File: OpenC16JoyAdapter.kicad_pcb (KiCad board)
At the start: 2 copper layers, 30.5 x 42.9 mm, 9 parts, among them J1 DB9 Male, P1 TO_C16_MINI_DIN_8, P2 PIN5_POWER, P3 OSHW_LOGO_PLACEHOLDER, P4 PULL_UP, U1 74LS244

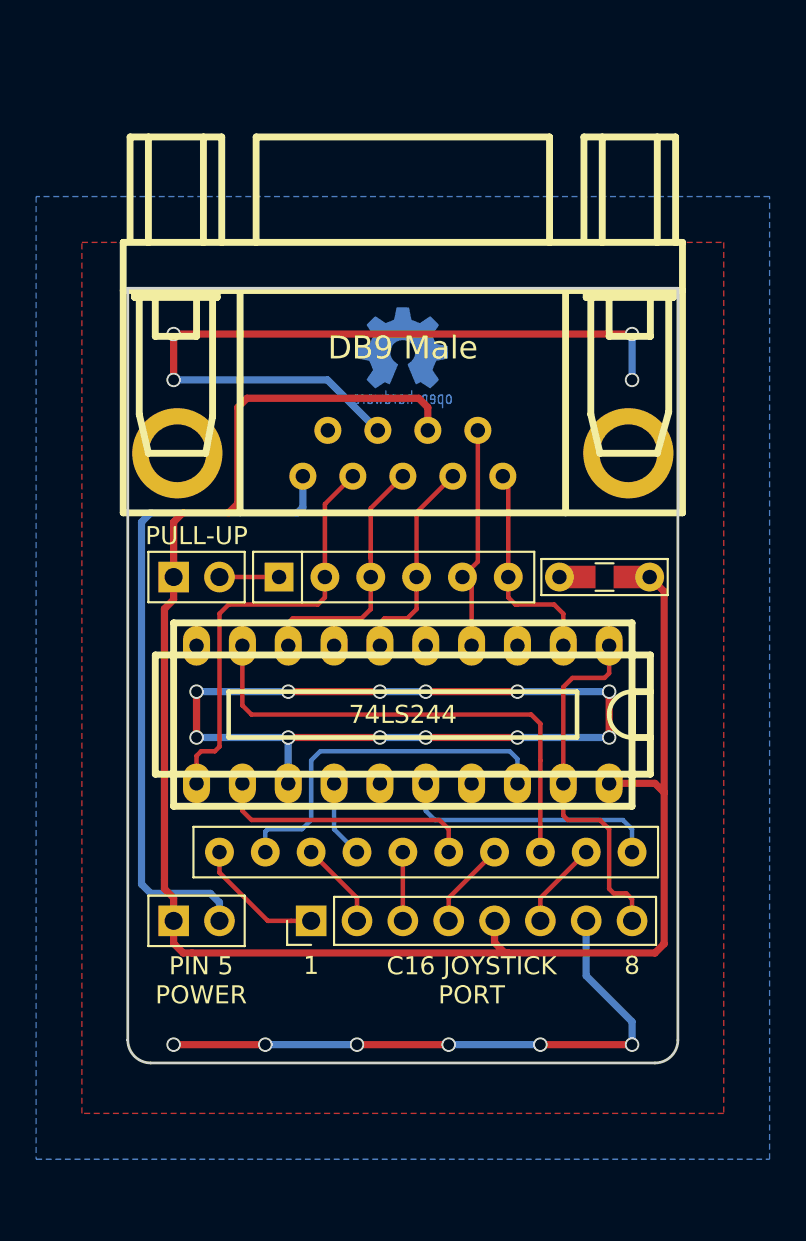
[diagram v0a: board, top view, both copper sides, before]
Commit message: Port to KiCad 5, remove pull-up jumper, tidy up, improve routing
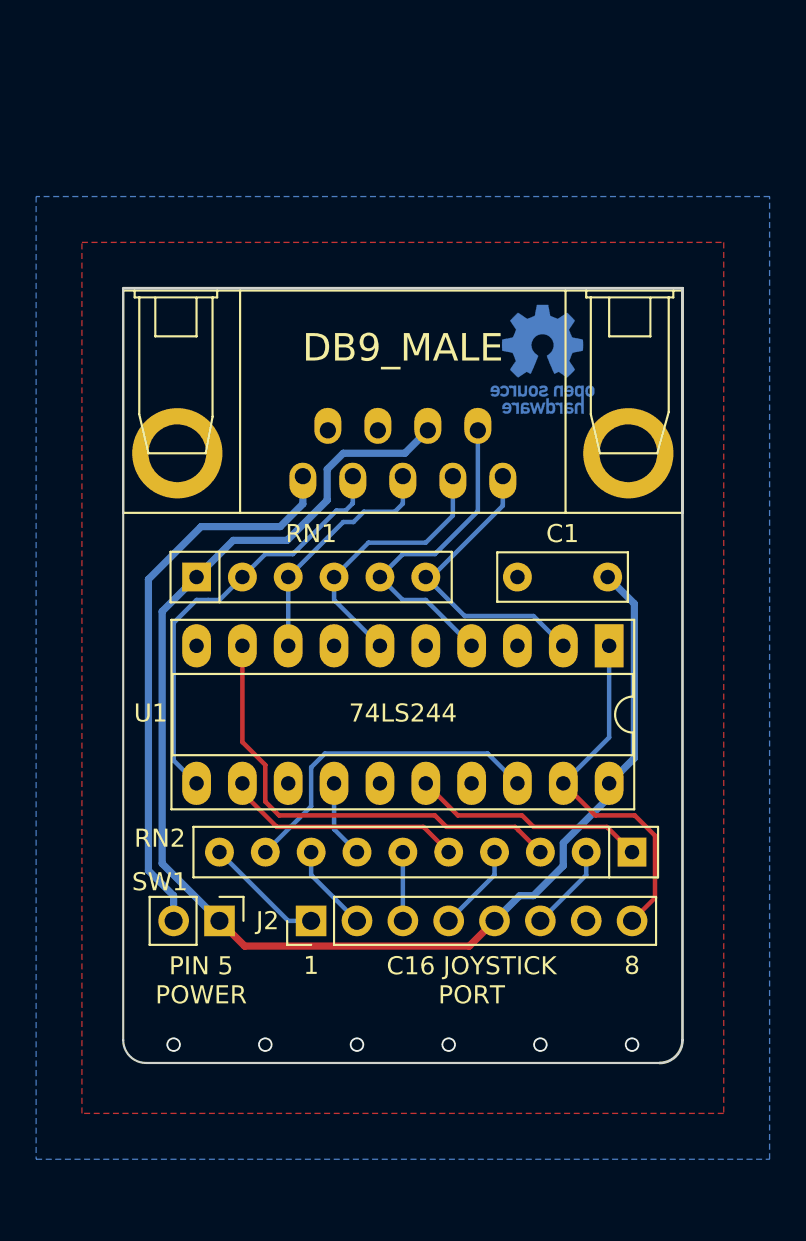
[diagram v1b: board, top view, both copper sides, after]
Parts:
- removed P1: TO_C16_MINI_DIN_8, Pin_Headers:Pin_Header_Straight_1x08_Pitch2.54mm
- removed P2: PIN5_POWER, OpenC16JoyAdapter:Pin_Header_Straight_1x02-ModSilkS
- removed P3: OSHW_LOGO_PLACEHOLDER, w_logo:Logo_copper_OSHW_6x6mm
- removed P4: PULL_UP, OpenC16JoyAdapter:Pin_Header_Straight_1x02-ModSilkS
- added J2: TO_C16_MINI_DIN_8, Connector_PinHeader_2.54mm:PinHeader_1x08_P2.54mm_Vertical, F.Cu at (142.2, 126.5)
- added SW1: PIN5_POWER, Connector_PinHeader_2.54mm:PinHeader_1x02_P2.54mm_Vertical, F.Cu at (137.2, 126.5)
- added V0: OSHW_LOGO, Symbol:OSHW-Logo_5.7x6mm_Copper, B.Cu at (155.1, 95.4)
- C1: footprint OpenC16JoyAdapter:C_0805+THT -> Capacitor_THT:C_Disc_D7.0mm_W2.5mm_P5.00mm
- J1: value DB9 Male -> DB9_MALE; footprint conn_d-sub:DB_9M -> OpenC16JoyAdapter:DB_9M
- RN1: footprint Resistors_THT:R_Array_SIP6 -> Resistor_THT:R_Array_SIP6
- RN2: footprint OpenC16JoyAdapter:R_Array_SIP10_NoPin1Mark -> Resistor_THT:R_Array_SIP10
- U1: footprint pth_circuits:dil_20-300_socket -> Package_DIP:DIP-20_W7.62mm_Socket_LongPads
- moved U1 12.0 mm to (158.8, 111.3), turned to 270 degrees
- moved RN1 4.57 mm to (135.9, 107.4)
- moved C1 0.17 mm to (158.7, 107.4)
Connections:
- J1 pad 9: (no net) -> /md_c_start
- RN1 pad 1: Net-(P4-Pad2) -> +5V
- U1 pad 3: (no net) -> Net-(U1-Pad3)
- U1 pad 5: (no net) -> Net-(U1-Pad5)
- U1 pad 7: (no net) -> Net-(U1-Pad7)
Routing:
- net GND: track 129.6 -> 0.00 mm, vias 22 -> 6
- net +5V: track 100.3 -> 78.1 mm
- net /md_b_~a: track 12.5 -> 18.1 mm
- net Net-(J1-Pad5): track 36.8 -> 31.3 mm
- net /md_up: track 12.0 -> 16.7 mm
- net Net-(P4-Pad2): track 3.30 -> 0.00 mm
- net /md_down: track 11.8 -> 15.0 mm
- net Net-(RN2-Pad9): track 20.4 -> 18.2 mm
- net Net-(RN2-Pad3): track 27.3 -> 25.6 mm
- net Net-(RN2-Pad1): track 14.6 -> 13.0 mm
- net Net-(RN2-Pad5): track 14.6 -> 13.3 mm
- net /md_left: track 14.5 -> 13.4 mm
- net /c16_up: track 7.32 -> 6.66 mm
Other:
- board size 30.5 x 42.9 mm -> 31 x 42.9 mm
- board text added: "+5V"
- board text added: "D"
- board text added: "F"
- board text added: "GND"
- board text added: "L"
- board text added: "Licensed under CERN OHL v.1.2"
- board text added: "R"
- board text added: "SEL"
- board text added: "U"
- board text added: "V3"
- board text removed: "PULL-UP"
- board text removed: "V2"

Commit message: Minor changes
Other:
- board text added: "Thanks to Levente Hársfalvi (TLC)!"

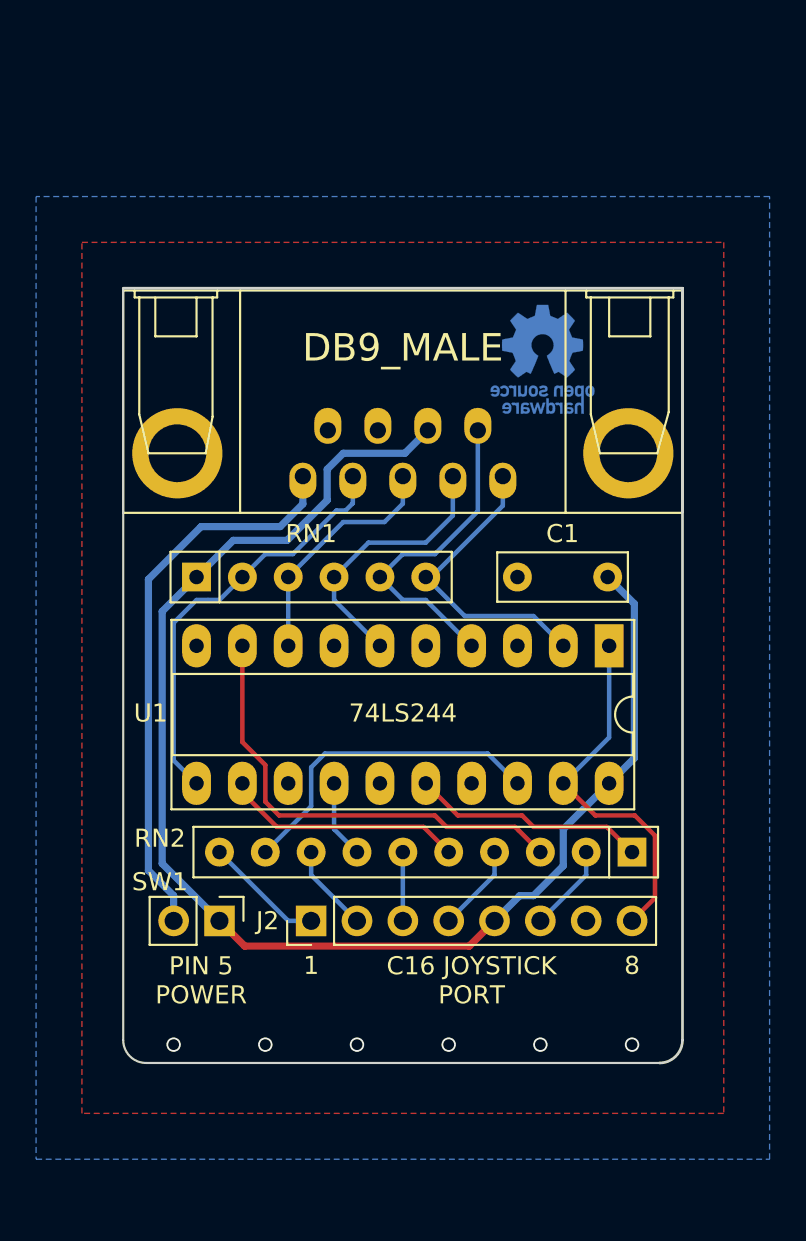
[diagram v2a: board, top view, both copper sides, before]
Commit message: Integrate light pen circuit
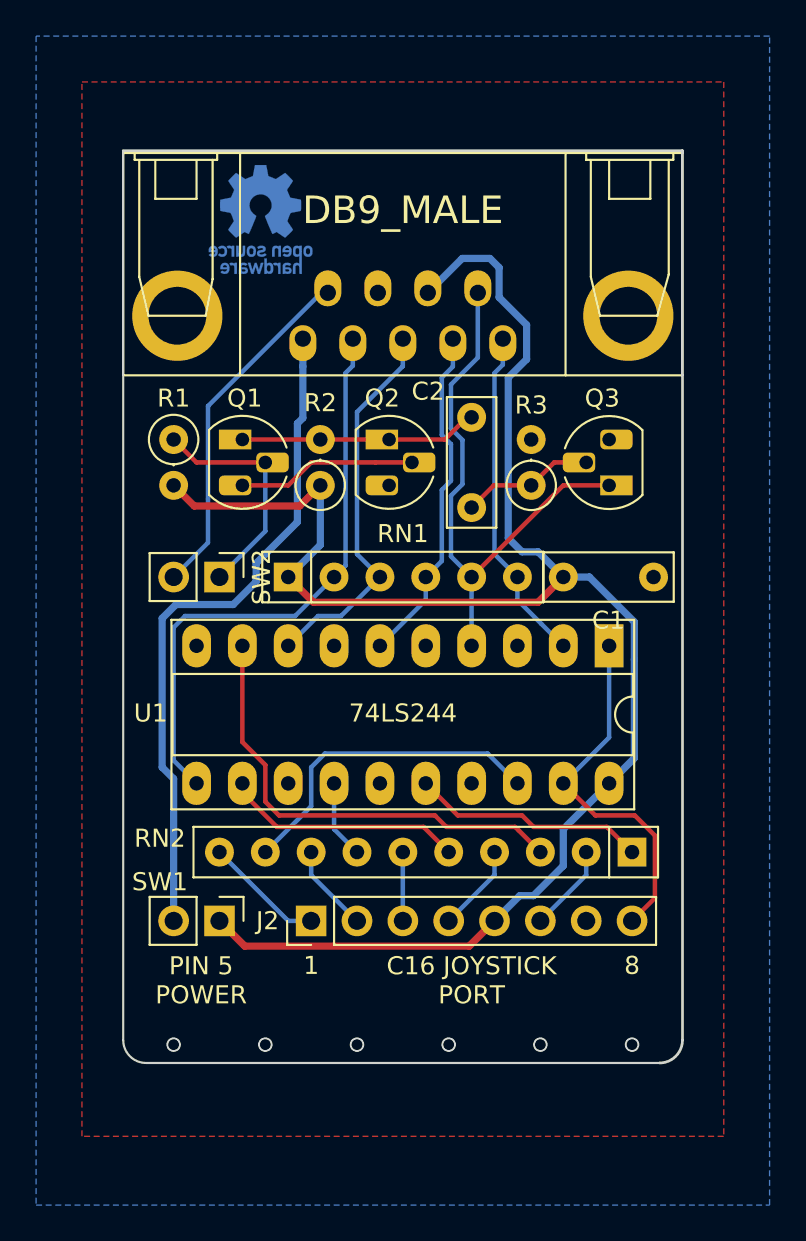
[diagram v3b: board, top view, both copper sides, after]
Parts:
- added C2: 220n, Capacitor_THT:C_Disc_D7.0mm_W2.5mm_P5.00mm, F.Cu at (151.1, 103.6)
- added Q1: BC548, Package_TO_SOT_THT:TO-92_HandSolder, F.Cu at (138.4, 99.8)
- added Q2: BC547, Package_TO_SOT_THT:TO-92_HandSolder, F.Cu at (146.6, 99.8)
- added Q3: BC547, Package_TO_SOT_THT:TO-92_HandSolder, F.Cu at (158.8, 102.4)
- added R1: 33k, Resistor_THT:R_Axial_DIN0207_L6.3mm_D2.5mm_P2.54mm_Vertical, F.Cu at (134.6, 99.8)
- added R2: 10k, Resistor_THT:R_Axial_DIN0207_L6.3mm_D2.5mm_P2.54mm_Vertical, F.Cu at (142.7, 102.4)
- added R3: 18k, Resistor_THT:R_Axial_DIN0207_L6.3mm_D2.5mm_P2.54mm_Vertical, F.Cu at (154.4, 102.4)
- added SW2: SW_LIGHTPEN, Connector_PinHeader_2.54mm:PinHeader_1x02_P2.54mm_Vertical, F.Cu at (137.2, 107.4)
- SW1: value PIN5_POWER -> SW_PIN5_POWER
- moved V0 17.4 mm to (139.4, 87.6)
- moved J1 7.62 mm to (147.3, 85.9)
- moved RN1 5.08 mm to (141.0, 107.4)
- moved C1 2.46 mm to (156.2, 107.4), turned to 0 degrees
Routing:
- net +5V: track 78.1 -> 97.8 mm
- net /md_c_start: track 0.00 -> 19.5 mm
- net Net-(Q1-Pad2): track 0.00 -> 13.0 mm
- net Net-(C2-Pad2): track 0.00 -> 13.0 mm
- net /md_b_~a: track 18.1 -> 30.9 mm
- net Net-(Q1-Pad3): track 0.00 -> 9.92 mm
- net /md_right: track 23.6 -> 32.8 mm
- net /md_left: track 13.4 -> 21.4 mm
- net Net-(C2-Pad1): track 0.00 -> 7.39 mm
- net Net-(J1-Pad5): track 31.3 -> 37.6 mm
- net /md_down: track 15.0 -> 19.4 mm
- net /md_up: track 16.7 -> 18.8 mm
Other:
- board size 31 x 42.9 mm -> 31 x 50.5 mm

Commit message: Add light pen circuit to PCB
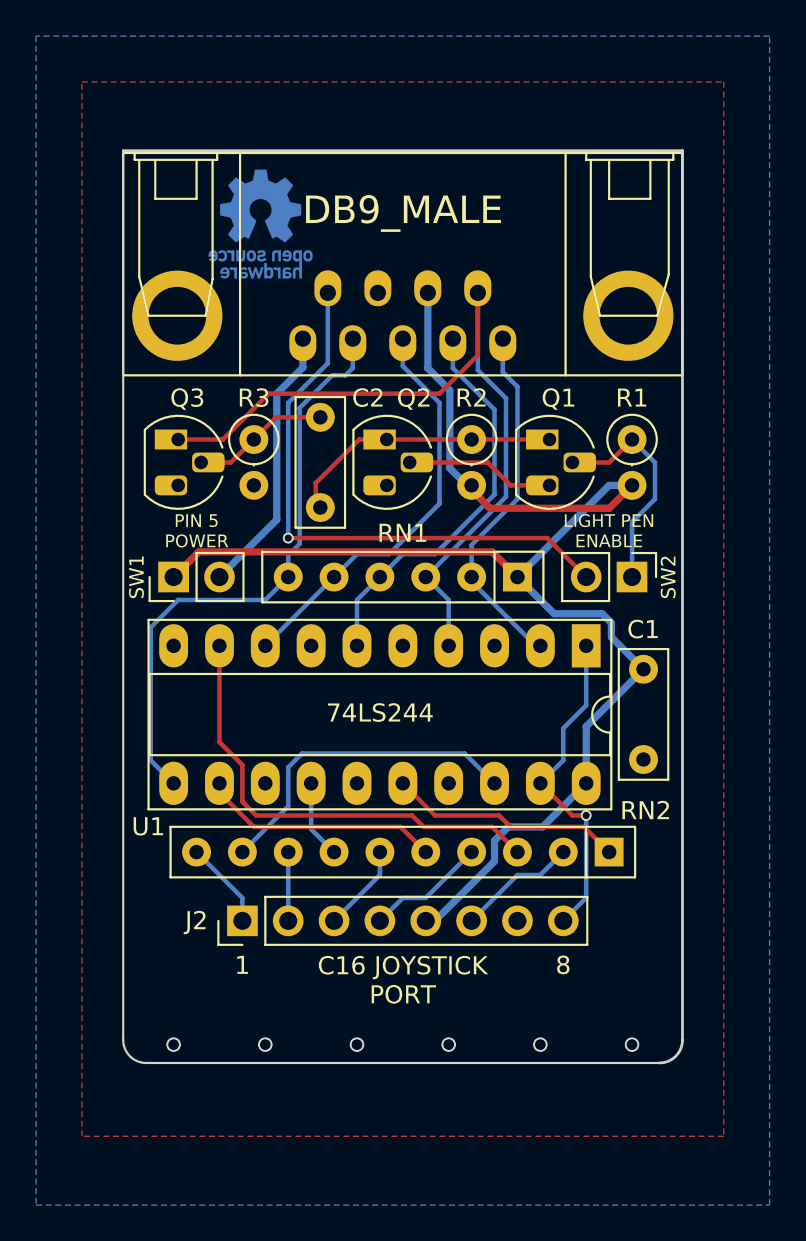
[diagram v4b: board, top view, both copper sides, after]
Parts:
- moved R1 25.4 mm to (160.0, 99.8)
- moved Q3 24.0 mm to (134.9, 99.8), turned to 270 degrees
- moved SW2 22.9 mm to (160.0, 107.4)
- moved SW1 19.2 mm to (134.6, 107.4), turned to 90 degrees
- moved Q1 17.0 mm to (155.4, 99.8)
- moved R3 15.6 mm to (139.1, 99.8), turned to 270 degrees
- moved RN1 12.7 mm to (153.7, 107.4), turned to 180 degrees
- moved C2 9.76 mm to (142.7, 98.6), turned to 270 degrees
- moved R2 8.76 mm to (151.1, 99.8), turned to 270 degrees
- moved C1 6.77 mm to (160.7, 112.6), turned to 270 degrees
- moved J2 3.81 mm to (138.4, 126.5)
- moved RN2 1.27 mm to (158.8, 122.7)
- moved U1 1.27 mm to (157.5, 111.3)
- moved V0 0.25 mm to (139.4, 87.9)
- moved Q2 0.13 mm to (146.4, 99.8)
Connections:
- R2 pad 1: +5V -> Net-(C2-Pad2)
- R2 pad 2: Net-(C2-Pad2) -> +5V
- RN1 pad 2: /md_right -> /md_up
- RN1 pad 3: /md_left -> /md_b_~a
- RN1 pad 5: /md_b_~a -> /md_left
- RN1 pad 6: /md_up -> /md_right
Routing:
- net Net-(J1-Pad5): track 37.6 -> 15.1 mm
- net +5V: track 97.8 -> 80.3 mm
- net /md_b_~a: track 30.9 -> 44.9 mm
- net /md_c_start: track 19.5 -> 31.9 mm, vias 0 -> 1
- net /md_down: track 19.4 -> 22.2 mm
- net Net-(Q1-Pad3): track 9.92 -> 7.51 mm
- net /c16_select: track 20.2 -> 18.3 mm, vias 0 -> 1
- net /c16_fire: track 4.86 -> 6.66 mm
- net /c16_right: track 4.86 -> 6.66 mm
- net /c16_up: track 6.66 -> 4.86 mm
- net Net-(C2-Pad2): track 13.0 -> 14.5 mm
- net /md_left: track 21.4 -> 22.9 mm
- net /md_up: track 18.8 -> 20.1 mm
- net /c16_left: track 3.81 -> 4.86 mm
- net /c16_down: track 4.86 -> 3.81 mm
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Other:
- board text added: "BTN"
- board text added: "LIGHT PEN ENABLE"
- board text added: "Thanks to Levente Hársfalvi (TLC) and LaViNa/Paul/Sacek of GOTU"
- board text removed: "F"
- board text removed: "Thanks to Levente Hársfalvi (TLC)!"

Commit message: Final touches
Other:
- board size 31 x 50.5 mm -> 31 x 50.4 mm
